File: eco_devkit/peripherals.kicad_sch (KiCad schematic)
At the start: 39 parts, among them J4 ADC_SEL1, J5 BluetoothHeader, Q1 MOSFET, Q2 MMBT3904, Q3 MOSFET, Q4 OP598A, SW3 PTS636, SW4 PTS636, SW5 PTS636, SW6 PTS636

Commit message: Atribui footprints.
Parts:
- R20, R28, R29: footprint (none) -> Resistor_SMD:R_0402_1005Metric
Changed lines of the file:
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@@
 			)
 		)
-		(property "Footprint" ""
+		(property "Footprint" "Resistor_SMD:R_0402_1005Metric"
 			(at 105.41 58.42 0)
 			(effects
@@
 			)
 		)
-		(property "Footprint" ""
+		(property "Footprint" "Resistor_SMD:R_0402_1005Metric"
 			(at 257.81 46.99 0)
 			(effects
@@
 			)
 		)
-		(property "Footprint" ""
+		(property "Footprint" "Resistor_SMD:R_0402_1005Metric"
 			(at 250.19 46.99 0)
 			(effects

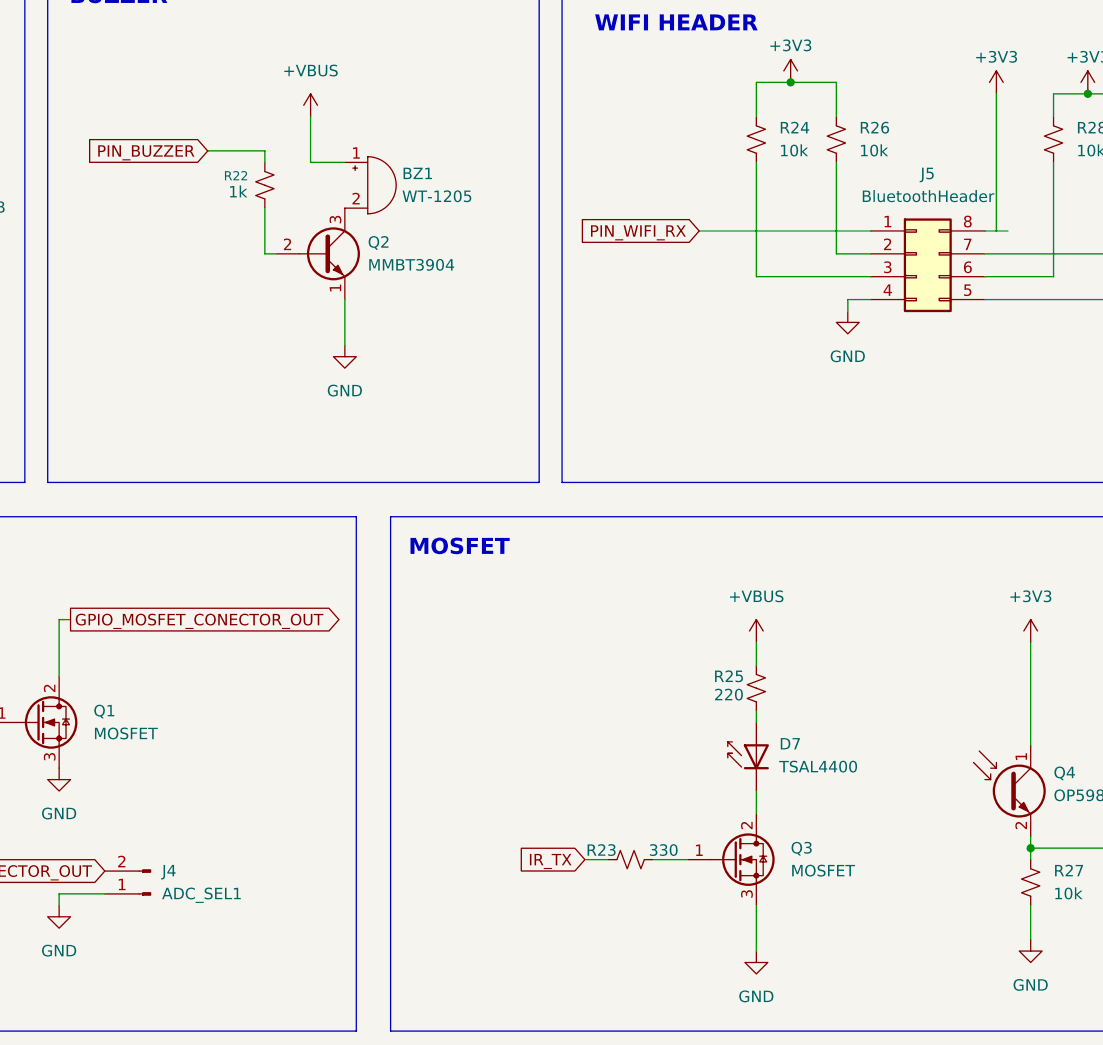
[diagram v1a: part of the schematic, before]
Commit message: Corrige footprints.
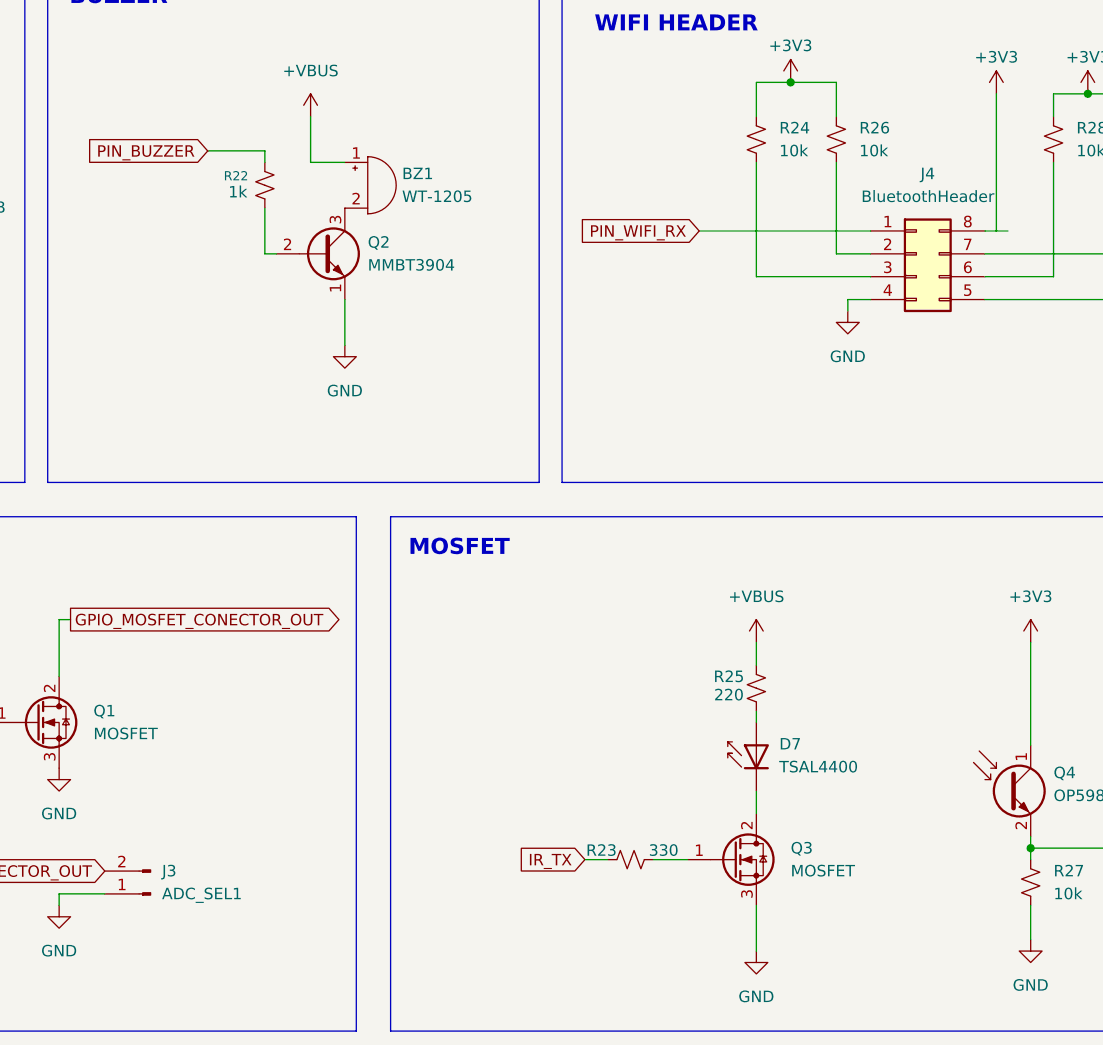
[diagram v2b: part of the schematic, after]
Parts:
- renumbered J4 to J3, J5 to J4
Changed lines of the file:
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@@
 		(on_board yes)
 		(dnp no)
-		(property "Reference" "J5"
+		(property "Reference" "J4"
 			(at 236.22 50.8 0)
 			(effects
@@
 			(project "eco_devkit"
 				(path "/308cd3d6-c3d9-49fe-9127-06fda61df52b/146c382c-2a6c-4a12-90a2-a26f2a1dd60b"
-					(reference "J5")
+					(reference "J4")
 					(unit 1)
 				)
@@
 		(dnp no)
 		(fields_autoplaced yes)
-		(property "Reference" "J4"
+		(property "Reference" "J3"
 			(at 151.13 128.2699 0)
 			(effects
@@
 			(project "eco_devkit"
 				(path "/308cd3d6-c3d9-49fe-9127-06fda61df52b/146c382c-2a6c-4a12-90a2-a26f2a1dd60b"
-					(reference "J4")
-					(unit 1)
-				)
+					(reference "J3")
+					(unit 1)
+				)

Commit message: footprint completed
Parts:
- BZ1: footprint Buzzer_Beeper:Buzzer_12mm_P5.0mm_Vertical -> lib:buzzer
- R13: MPN RCS0402120RFKED -> CRCW0402150RFKEDHP
- R15: MPN AC0402FR-7W130RL -> CRCW0402150RFKEDHP
- R22: MPN (none) -> CRCW04021K00FKED
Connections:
- net +3V3: now also J4.8 (Pin_8)
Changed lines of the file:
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@@
 	(wire
 		(pts
-			(xy 245.11 57.15) (xy 242.57 57.15)
+			(xy 250.19 49.53) (xy 250.19 62.23)
 		)
 		(stroke
@@
 	(wire
 		(pts
-			(xy 250.19 49.53) (xy 250.19 62.23)
+			(xy 167.64 49.53) (xy 167.64 44.45)
 		)
 		(stroke
@@
 	(wire
 		(pts
-			(xy 167.64 49.53) (xy 167.64 44.45)
+			(xy 46.99 119.38) (xy 46.99 118.11)
 		)
 		(stroke
@@
 	(wire
 		(pts
-			(xy 46.99 119.38) (xy 46.99 118.11)
+			(xy 156.21 48.26) (xy 162.56 48.26)
 		)
 		(stroke
@@
 	(wire
 		(pts
-			(xy 156.21 48.26) (xy 162.56 48.26)
+			(xy 46.99 127) (xy 60.96 127)
 		)
 		(stroke
@@
 	(wire
 		(pts
-			(xy 46.99 127) (xy 60.96 127)
+			(xy 242.57 57.15) (xy 243.84 57.15)
 		)
 		(stroke
@@
 			)
 		)
-		(property "Datasheet" "https://www.digikey.com.br/en/products/detail/vishay-dale/RCS0402120RFKED/5867593"
+		(property "Datasheet" "https://www.digikey.com.br/en/products/detail/vishay-dale/CRCW0402150RFKEDHP/2225278"
 			(at 38.1 57.15 0)
 			(effects
@@
 			)
 		)
-		(property "MPN" "RCS0402120RFKED"
+		(property "MPN" "CRCW0402150RFKEDHP"
 			(at 38.1 57.15 90)
 			(effects
@@
 			)
 		)
+		(property "MPN" "CRCW04021K00FKED"
+			(at 162.56 52.07 0)
+			(effects
+				(font
+					(size 1.27 1.27)
+				)
+				(hide yes)
+			)
+		)
 		(pin "1"
 		)
@@
 			)
 		)
-		(property "Footprint" "Buzzer_Beeper:Buzzer_12mm_P5.0mm_Vertical"
+		(property "Footprint" "lib:buzzer"
 			(at 173.355 49.53 90)
 			(effects
@@
 			)
 		)
-		(property "Datasheet" "https://www.digikey.com.br/en/products/detail/yageo/AC0402FR-7W130RL/17014632"
+		(property "Datasheet" "https://www.digikey.com.br/en/products/detail/vishay-dale/CRCW0402150RFKEDHP/2225278"
 			(at 38.1 77.47 0)
 			(effects
@@
 			)
 		)
-		(property "MPN" "AC0402FR-7W130RL"
+		(property "MPN" "CRCW0402150RFKEDHP"
 			(at 38.1 77.47 90)
 			(effects
